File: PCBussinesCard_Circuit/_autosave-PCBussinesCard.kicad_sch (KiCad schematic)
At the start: 17 parts, among them IC1 NT2H1311F0DTL, J1 Conn_ARM_JTAG_SWD_10, J2 USB_A_PCB, J3 Conn_01x13_Pin, J4 Conn_01x13_Pin, U1 STM32L552CCTx, U2 AP7370-33FDC

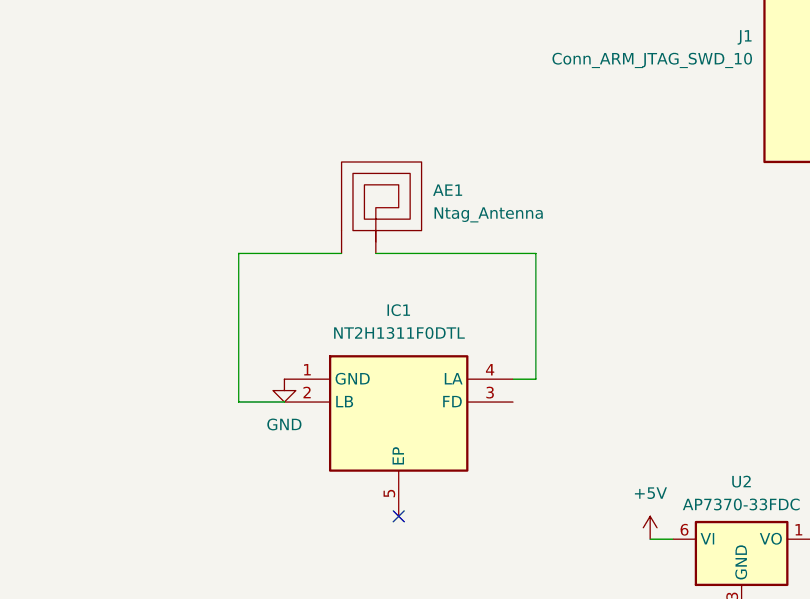
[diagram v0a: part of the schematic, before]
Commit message: fixed nfc antena
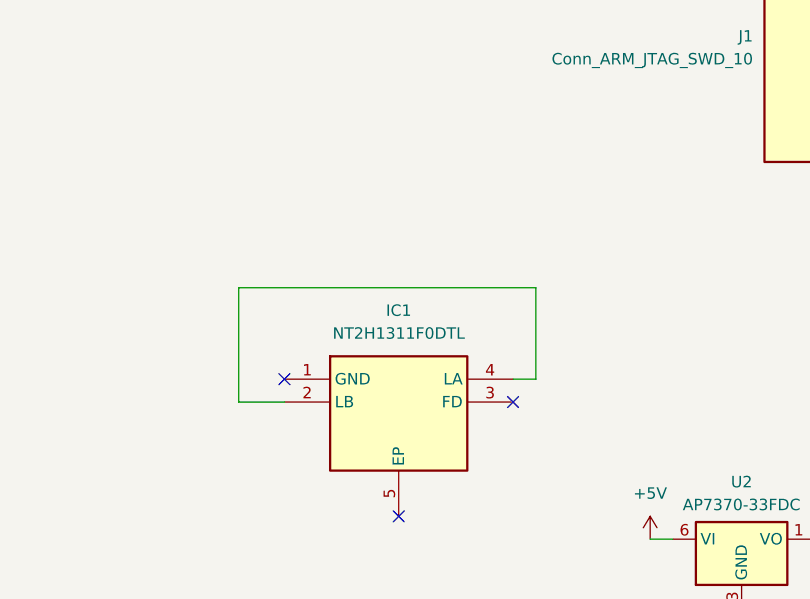
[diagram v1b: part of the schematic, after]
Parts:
- removed AE1: Ntag_Antenna, ProjectLibrary:Ntag_Antenna, symbol Project_library:Ntag_Antenna
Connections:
- net GND: no longer IC1.1 (GND)
- net at IC1.2 (LB): now also IC1.4 (LA)
- no-connect marks 3 -> 5
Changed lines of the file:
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@@
+	)
+	(no_connect
+		(at 125.73 82.55)
 	)
 	(no_connect
@@
 	)
 	(no_connect
+		(at 151.13 85.09)
+	)
+	(no_connect
 		(at 201.93 48.26)
 	)
@@
 	(wire
 		(pts
+			(xy 120.65 85.09) (xy 120.65 72.39)
+		)
+		(stroke
+			(width 0)
+			(type default)
+		)
+	)
+	(wire
+		(pts
 			(xy 41.91 34.29) (xy 50.8 34.29)
 		)
@@
 	(wire
 		(pts
+			(xy 120.65 72.39) (xy 153.67 72.39)
+		)
+		(stroke
+			(width 0)
+			(type default)
+		)
+	)
+	(wire
+		(pts
 			(xy 67.31 105.41) (xy 68.58 105.41)
 		)
@@
 	(wire
 		(pts
-			(xy 120.65 85.09) (xy 120.65 68.58)
-		)
-		(stroke
-			(width 0)
-			(type default)
-		)
-	)
-	(wire
-		(pts
 			(xy 81.28 69.85) (xy 90.17 69.85)
 		)
@@
 	(wire
 		(pts
-			(xy 120.65 68.58) (xy 132.08 68.58)
-		)
-		(stroke
-			(width 0)
-			(type default)
-		)
-	)
-	(wire
-		(pts
 			(xy 68.58 26.67) (xy 71.12 26.67)
 		)
@@
 	(wire
 		(pts
-			(xy 153.67 82.55) (xy 153.67 68.58)
-		)
-		(stroke
-			(width 0)
-			(type default)
-		)
-	)
-	(wire
-		(pts
 			(xy 201.93 38.1) (xy 209.55 38.1)
 		)
@@
 	(wire
 		(pts
-			(xy 153.67 68.58) (xy 135.89 68.58)
+			(xy 153.67 72.39) (xy 153.67 82.55)
 		)
 		(stroke
@@
 					(unit 1)
 				)
-			)
-		)
-	)
-	(symbol
-		(lib_id "power:GND")
-		(at 125.73 82.55 0)
-		(unit 1)
-		(exclude_from_sim no)
-		(in_bom yes)
-		(on_board yes)
-		(dnp no)
-		(fields_autoplaced yes)
-		(property "Reference" "#PWR013"
-			(at 125.73 88.9 0)
-			(effects
-				(font
-					(size 1.27 1.27)
-				)
-				(hide yes)
-			)
-		)
-		(property "Value" "GND"
-			(at 125.73 87.63 0)
-			(effects
-				(font
-					(size 1.27 1.27)
-				)
-			)
-		)
-		(property "Footprint" ""
-			(at 125.73 82.55 0)
-			(effects
-				(font
-					(size 1.27 1.27)
-				)
-				(hide yes)
-			)
-		)
-		(property "Datasheet" ""
-			(at 125.73 82.55 0)
-			(effects
-				(font
-					(size 1.27 1.27)
-				)
-				(hide yes)
-			)
-		)
-		(property "Description" "Power symbol creates a global label with name \"GND\" , ground"
-			(at 125.73 82.55 0)
-			(effects
-				(font
-					(size 1.27 1.27)
-				)
-				(hide yes)
-			)
-		)
-		(pin "1"
-		)
-		(instances
-			(project "PCBussinesCard"
-				(path "/e246fc9e-4f6b-4825-8175-4f9f8724cfc1"
-					(reference "#PWR013")
-					(unit 1)
-				)
-			)
-		)
-	)
-	(symbol
-		(lib_id "Project_library:Ntag_Antenna")
-		(at 135.89 63.5 0)
-		(unit 1)
-		(exclude_from_sim no)
-		(in_bom yes)
-		(on_board yes)
-		(dnp no)
-		(fields_autoplaced yes)
-		(property "Reference" "AE1"
-			(at 142.24 61.5949 0)
-			(effects
-				(font
-					(size 1.27 1.27)
-				)
-				(justify left)
-			)
-		)
-		(property "Value" "Ntag_Antenna"
-			(at 142.24 64.1349 0)
-			(effects
-				(font
-					(size 1.27 1.27)
-				)
-				(justify left)
-			)
-		)
-		(property "Footprint" "ProjectLibrary:Ntag_Antenna"
-			(at 135.89 63.5 0)
-			(effects
-				(font
-					(size 1.27 1.27)
-				)
-				(hide yes)
-			)
-		)
-		(property "Datasheet" "~"
-			(at 135.89 63.5 0)
-			(effects
-				(font
-					(size 1.27 1.27)
-				)
-				(hide yes)
-			)
-		)
-		(property "Description" "Loop antenna"
-			(at 137.16 57.15 0)
-			(effects
-				(font
-					(size 1.27 1.27)
-				)
-				(hide yes)
-			)
-		)
-		(pin "2"
-		)
-		(pin "1"
-		)
-		(instances
-			(project ""
-				(path "/e246fc9e-4f6b-4825-8175-4f9f8724cfc1"
-					(reference "AE1")
-					(unit 1)
-				)
